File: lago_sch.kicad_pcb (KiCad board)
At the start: 2 copper layers, 98.9 x 84.4 mm, 132 parts, among them J1 DB15, J2 DB15, J3 BARREL_JACK, J4 HEADER_16, P1 Conn_GPS, P2 Conn_BMP280, P3 I2C_EXT, P4 I2C_EXT, P5 CONN_01X06, P6 CONN_01X04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

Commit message: Agrgeo la version para kicad v6
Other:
- net class Default removed
- net class power removed
- net class sw_power removed

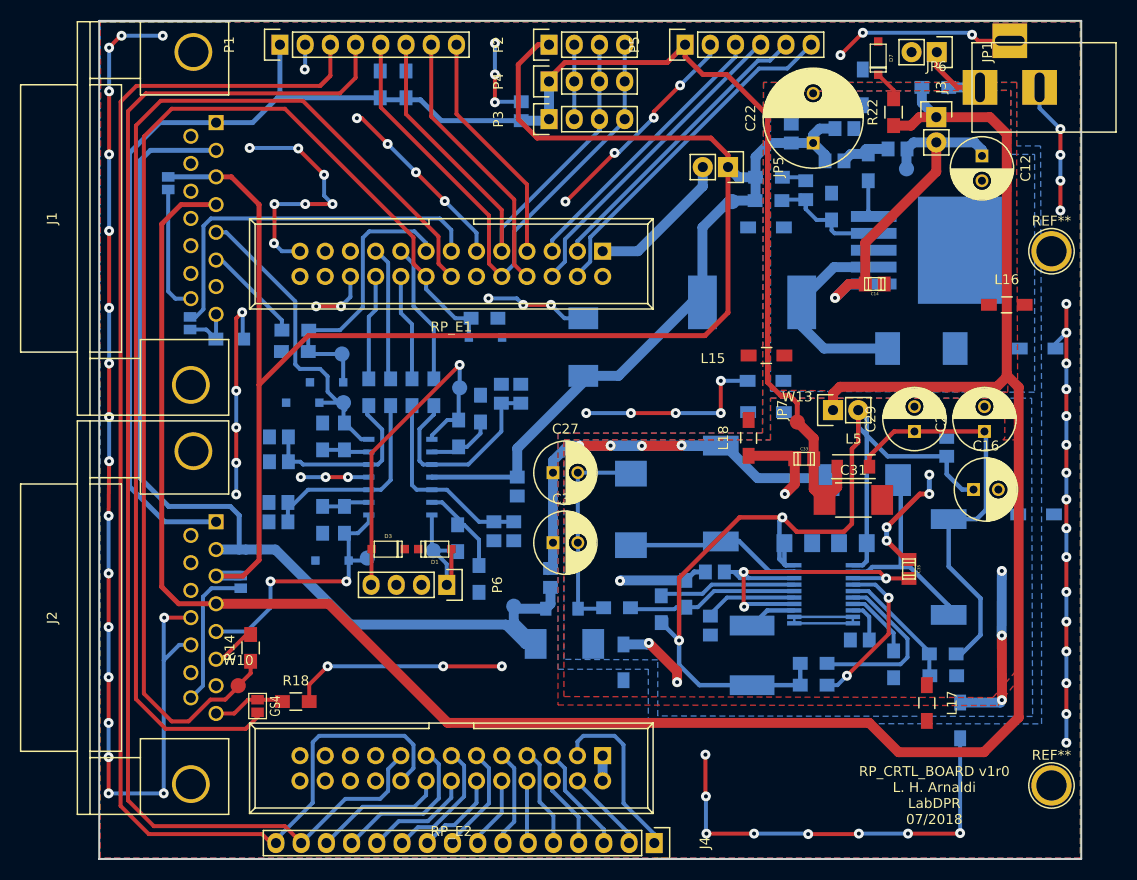
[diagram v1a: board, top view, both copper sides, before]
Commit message: Agrego la version modificada para Mario de Ecuador, con vias mas grandes
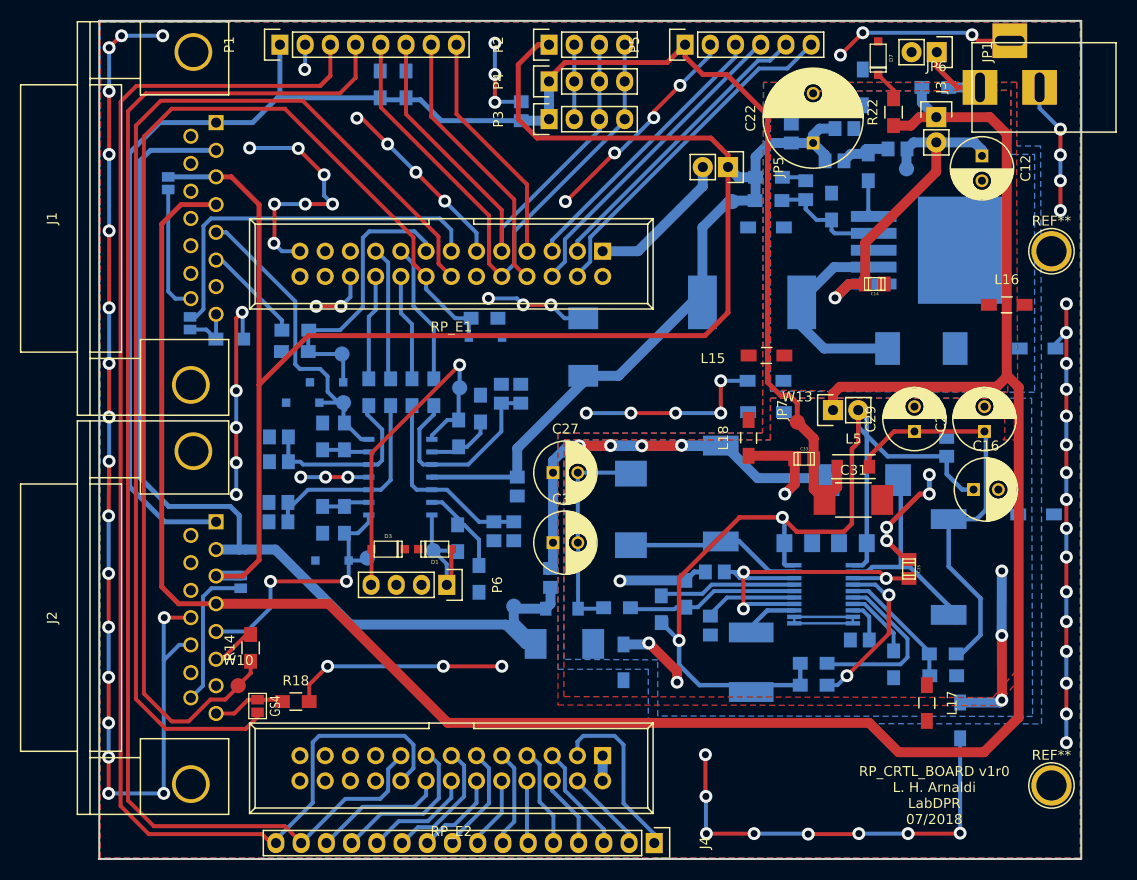
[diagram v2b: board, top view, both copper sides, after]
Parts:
- moved L1 0.70 mm to (116.8, 114.6)
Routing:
- net Net-(R29-Pad1): track 16.1 -> 20.5 mm
- net Net-(C15-Pad1): track 101.8 -> 99.7 mm
- net Net-(C18-Pad1): track 39.1 -> 40.1 mm
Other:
- rule pad_to_mask_clearance: 0.2 -> 0

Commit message: Actualicé el pcb con los valores del esquemático
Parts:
- C16: value 100u -> 47u
- R1, R2, R3, R32, R34, R4: value 68.1k -> 68k
- R10, R11, R12, R9: value 100k -> 220k
- R13, R14: value 12.1k -> 12k
- R15, R16: value 33.2k -> 33k
- R22: value 470 -> 560
- R24: value 174K -> 180K
- R25: value 3k -> 3k3
- R27: value 182K -> 180K
- R31, R33: value 215k -> 220k
- R5, R6, R7, R8: value 249k -> 100k
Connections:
- J1 pad 14: Net-(J1-Pad14) -> unconnected-(J1-Pad14)
- J1 pad 7: Net-(J1-Pad7) -> unconnected-(J1-Pad7)
- J2 pad 14: Net-(J2-Pad14) -> unconnected-(J2-Pad14)
- J2 pad 7: Net-(J2-Pad7) -> unconnected-(J2-Pad7)
- RP_E1 pad 2: Net-(RP_E1-Pad2) -> unconnected-(RP_E1-Pad2)
- RP_E1 pad 23: Net-(RP_E1-Pad23) -> unconnected-(RP_E1-Pad23)
- RP_E1 pad 24: Net-(RP_E1-Pad24) -> unconnected-(RP_E1-Pad24)
- RP_E2 pad 19: Net-(RP_E2-Pad19) -> unconnected-(RP_E2-Pad19)
- RP_E2 pad 20: Net-(RP_E2-Pad20) -> unconnected-(RP_E2-Pad20)
- RP_E2 pad 21: Net-(RP_E2-Pad21) -> unconnected-(RP_E2-Pad21)
- RP_E2 pad 22: Net-(RP_E2-Pad22) -> unconnected-(RP_E2-Pad22)
- RP_E2 pad 23: Net-(RP_E2-Pad23) -> unconnected-(RP_E2-Pad23)
- RP_E2 pad 24: Net-(RP_E2-Pad24) -> unconnected-(RP_E2-Pad24)
